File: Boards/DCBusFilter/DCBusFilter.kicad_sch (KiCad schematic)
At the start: 8 parts, among them J1 TBP01R2-508-04BE, J2 TBP01R2-508-04BE

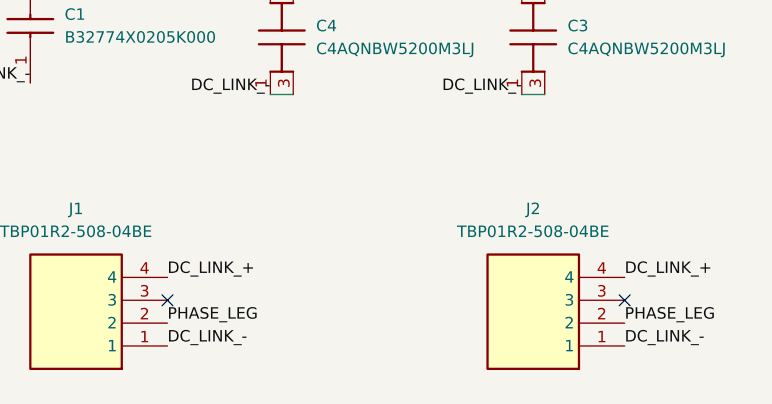
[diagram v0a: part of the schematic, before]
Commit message: layout control boards, add baseplate, refine mechanical layout
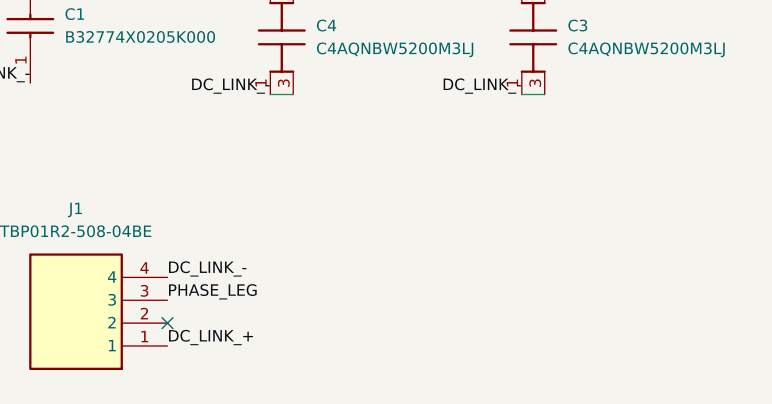
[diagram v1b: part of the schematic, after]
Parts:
- removed J2: TBP01R2-508-04BE, SHDR4W100P0X508_1X4_2192X850X1200P, symbol InverterCom:TBP01R2-508-04BE
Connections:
- net DC_LINK_+: now also J1.1; no longer J1.4
- net DC_LINK_-: now also J1.4; no longer J1.1
- net PHASE_LEG: now also J1.3; no longer J1.2
- no-connect marks 2 -> 1
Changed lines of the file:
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@@
 	(paper "A4")
 	(no_connect
-		(at 91.44 81.28)
-	)
-	(no_connect
-		(at 142.24 81.28)
+		(at 91.44 83.82)
 	)
 	(wire
@@
 		)
 	)
-	(label "DC_LINK_-"
-		(at 142.24 86.36 0)
-		(effects
-			(font
-				(size 1.27 1.27)
-			)
-			(justify left bottom)
-		)
-	)
-	(label "DC_LINK_-"
+	(label "DC_LINK_+"
 		(at 91.44 86.36 0)
-		(effects
-			(font
-				(size 1.27 1.27)
-			)
-			(justify left bottom)
-		)
-	)
-	(label "PHASE_LEG"
-		(at 91.44 83.82 0)
 		(effects
 			(font
@@
 		)
 	)
-	(label "DC_LINK_+"
-		(at 91.44 78.74 0)
-		(effects
-			(font
-				(size 1.27 1.27)
-			)
-			(justify left bottom)
-		)
-	)
 	(label "PHASE_LEG"
 		(at 38.1 88.9 0)
@@
 		)
 	)
-	(label "DC_LINK_+"
-		(at 142.24 78.74 0)
-		(effects
-			(font
-				(size 1.27 1.27)
-			)
-			(justify left bottom)
-		)
-	)
 	(label "DC_LINK_-"
 		(at 102.87 58.42 180)
@@
 	)
 	(label "DC_LINK_-"
+		(at 91.44 78.74 0)
+		(effects
+			(font
+				(size 1.27 1.27)
+			)
+			(justify left bottom)
+		)
+	)
+	(label "DC_LINK_-"
 		(at 38.1 63.5 0)
+		(effects
+			(font
+				(size 1.27 1.27)
+			)
+			(justify left bottom)
+		)
+	)
+	(label "PHASE_LEG"
+		(at 91.44 81.28 0)
 		(effects
 			(font
@@
 	(label "DC_LINK_+"
 		(at 38.1 38.1 0)
-		(effects
-			(font
-				(size 1.27 1.27)
-			)
-			(justify left bottom)
-		)
-	)
-	(label "PHASE_LEG"
-		(at 142.24 83.82 0)
 		(effects
 			(font
@@
 					(unit 1)
 				)
-			)
-		)
-	)
-	(symbol
-		(lib_id "InverterCom:TBP01R2-508-04BE")
-		(at 142.24 86.36 180)
-		(unit 1)
-		(exclude_from_sim no)
-		(in_bom yes)
-		(on_board yes)
-		(dnp no)
-		(fields_autoplaced yes)
-		(property "Reference" "J2"
-			(at 132.08 71.12 0)
-			(effects
-				(font
-					(size 1.27 1.27)
-				)
-			)
-		)
-		(property "Value" "TBP01R2-508-04BE"
-			(at 132.08 73.66 0)
-			(effects
-				(font
-					(size 1.27 1.27)
-				)
-			)
-		)
-		(property "Footprint" "SHDR4W100P0X508_1X4_2192X850X1200P"
-			(at 125.73 -8.56 0)
-			(effects
-				(font
-					(size 1.27 1.27)
-				)
-				(justify left top)
-				(hide yes)
-			)
-		)
-		(property "Datasheet" "https://www.sameskydevices.com/product/resource/tbp01r2-508.pdf"
-			(at 125.73 -108.56 0)
-			(effects
-				(font
-					(size 1.27 1.27)
-				)
-				(justify left top)
-				(hide yes)
-			)
-		)
-		(property "Description" "TBP01R2-508 Series - 2~24 Poles, Pluggable, Receptacle, Vertical, 5.08 Pitch, Terminal Block Connector"
-			(at 142.24 86.36 0)
-			(effects
-				(font
-					(size 1.27 1.27)
-				)
-				(hide yes)
-			)
-		)
-		(property "Height" "12"
-			(at 125.73 -308.56 0)
-			(effects
-				(font
-					(size 1.27 1.27)
-				)
-				(justify left top)
-				(hide yes)
-			)
-		)
-		(property "Mouser Part Number" "490-TBP01R2-508-04BE"
-			(at 125.73 -408.56 0)
-			(effects
-				(font
-					(size 1.27 1.27)
-				)
-				(justify left top)
-				(hide yes)
-			)
-		)
-		(property "Mouser Price/Stock" "https://www.mouser.co.uk/ProductDetail/CUI-Devices/TBP01R2-508-04BE?qs=PzGy0jfpSMt81U9Qkgbf1g%3D%3D"
-			(at 125.73 -508.56 0)
-			(effects
-				(font
-					(size 1.27 1.27)
-				)
-				(justify left top)
-				(hide yes)
-			)
-		)
-		(property "Manufacturer_Name" "Same Sky"
-			(at 125.73 -608.56 0)
-			(effects
-				(font
-					(size 1.27 1.27)
-				)
-				(justify left top)
-				(hide yes)
-			)
-		)
-		(property "Manufacturer_Part_Number" "TBP01R2-508-04BE"
-			(at 125.73 -708.56 0)
-			(effects
-				(font
-					(size 1.27 1.27)
-				)
-				(justify left top)
-				(hide yes)
-			)
-		)
-		(pin "2"
-		)
-		(pin "1"
-		)
-		(pin "3"
-		)
-		(pin "4"
-		)
-		(instances
-			(project "DCBusFilter"
-				(path "/2365f093-f079-4cf2-9926-0ba7dd4b2726"
-					(reference "J2")
-					(unit 1)
-				)

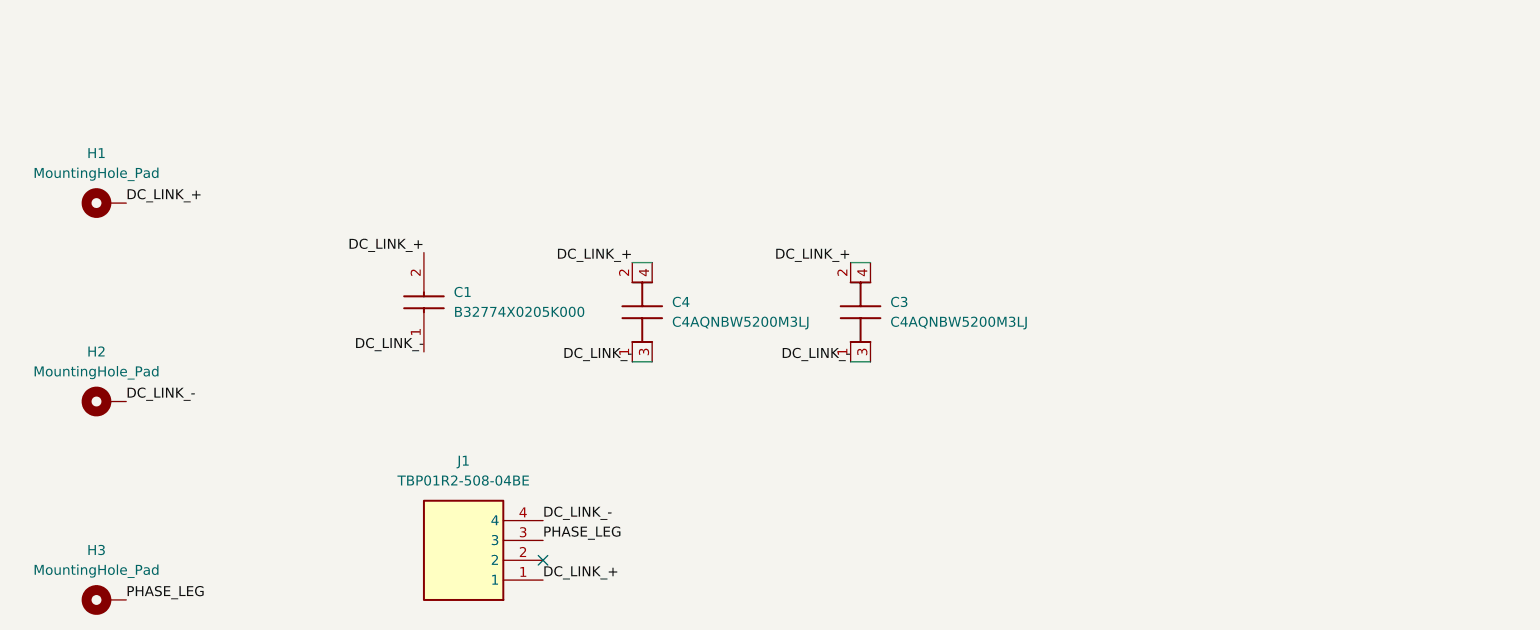
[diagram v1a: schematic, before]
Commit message: Layout mainboard, add EMI filter caps
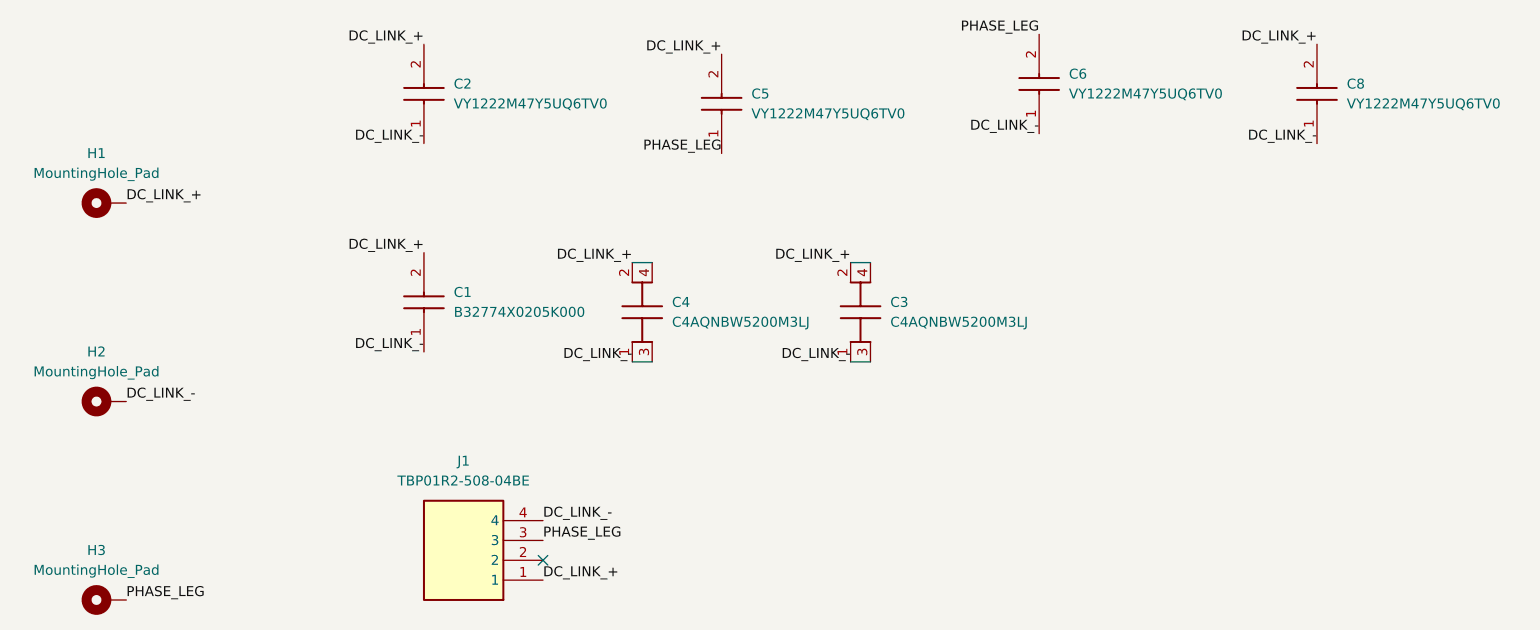
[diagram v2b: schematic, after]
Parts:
- added C2, C5, C6, C8: VY1222M47Y5UQ6TV0, VY1222M47Y5UQ6TV0, symbol InverterCom:VY1222M47Y5UQ6TV0
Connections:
- net DC_LINK_+: now also C2.2, C5.2, C8.2
- net DC_LINK_-: now also C2.1, C6.1, C8.1
- net PHASE_LEG: now also C5.1, C6.2
